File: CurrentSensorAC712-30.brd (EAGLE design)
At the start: 48 x 24 mm, 9 parts, among them IC1 ACS758LCB-050B-PFF-T

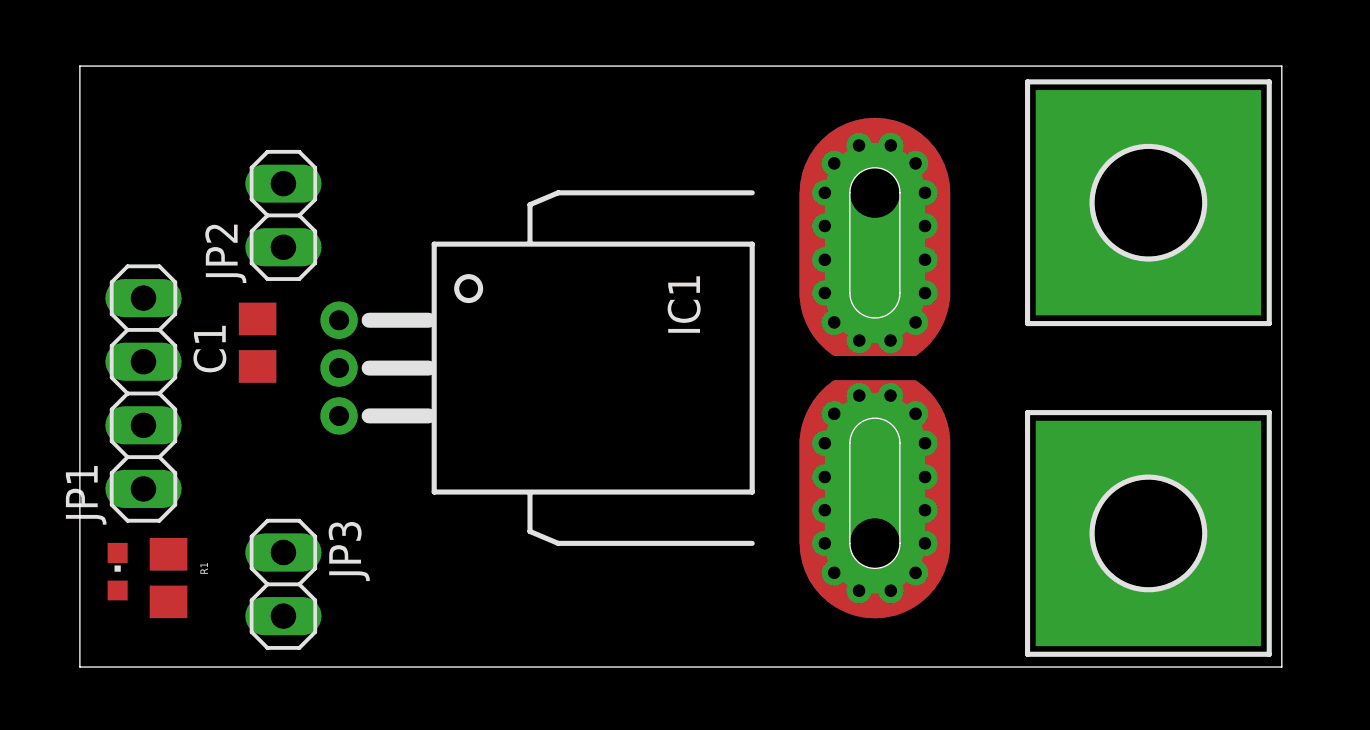
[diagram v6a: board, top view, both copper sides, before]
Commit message: sensor ACS758 layouted
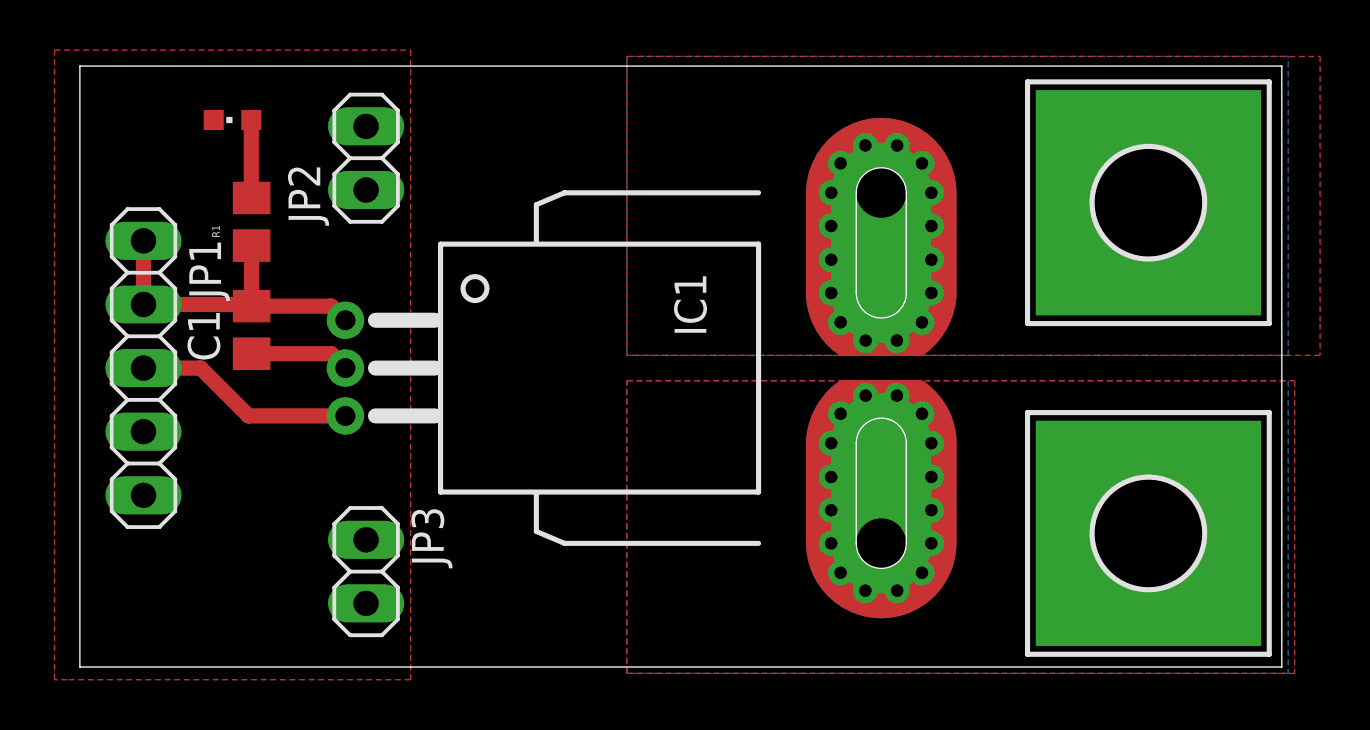
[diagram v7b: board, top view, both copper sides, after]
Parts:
- JP1: device pinhead:1X04 -> pinhead:1X05
- moved LED1 18.6 mm to (6.10, 21.8), turned to 90 degrees
- moved R1 14.6 mm to (6.86, 17.8), turned to 90 degrees
- moved JP2 4.02 mm to (11.4, 20.3)
- moved JP3 3.34 mm to (11.4, 3.81)
- moved JP1 1.02 mm to (2.54, 11.9), turned to 270 degrees
- moved C1 0.56 mm to (6.86, 13.5)
- moved IC1 0.25 mm to (32.0, 11.9)
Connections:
- net 5VDC: now also JP1.2
- net GND: now also JP1.5; no longer JP1.3
- net N$6: now also JP1.3; no longer JP1.2
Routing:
- net 5VDC: track 0.00 -> 13.3 mm
- net N$6: track 0.00 -> 8.86 mm
- net GND: track 0.00 -> 3.98 mm
- net N$5: track 0.00 -> 3.12 mm
- added copper zone on layer 1, net GND
- added copper zone on layer 1, net IN
- added copper zone on layer 16, net IN
- added copper zone on layer 1, net OUT
- added copper zone on layer 16, net OUT
